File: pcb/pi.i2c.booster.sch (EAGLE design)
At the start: 41 parts, among them M328 ATMEGA328P-AU, SW1 RJ45SMD, SW2 RJ45SMD, SW3 RJ45SMD, T1 IRFR5305, T2 BC847BSMD, T3 BC847BSMD

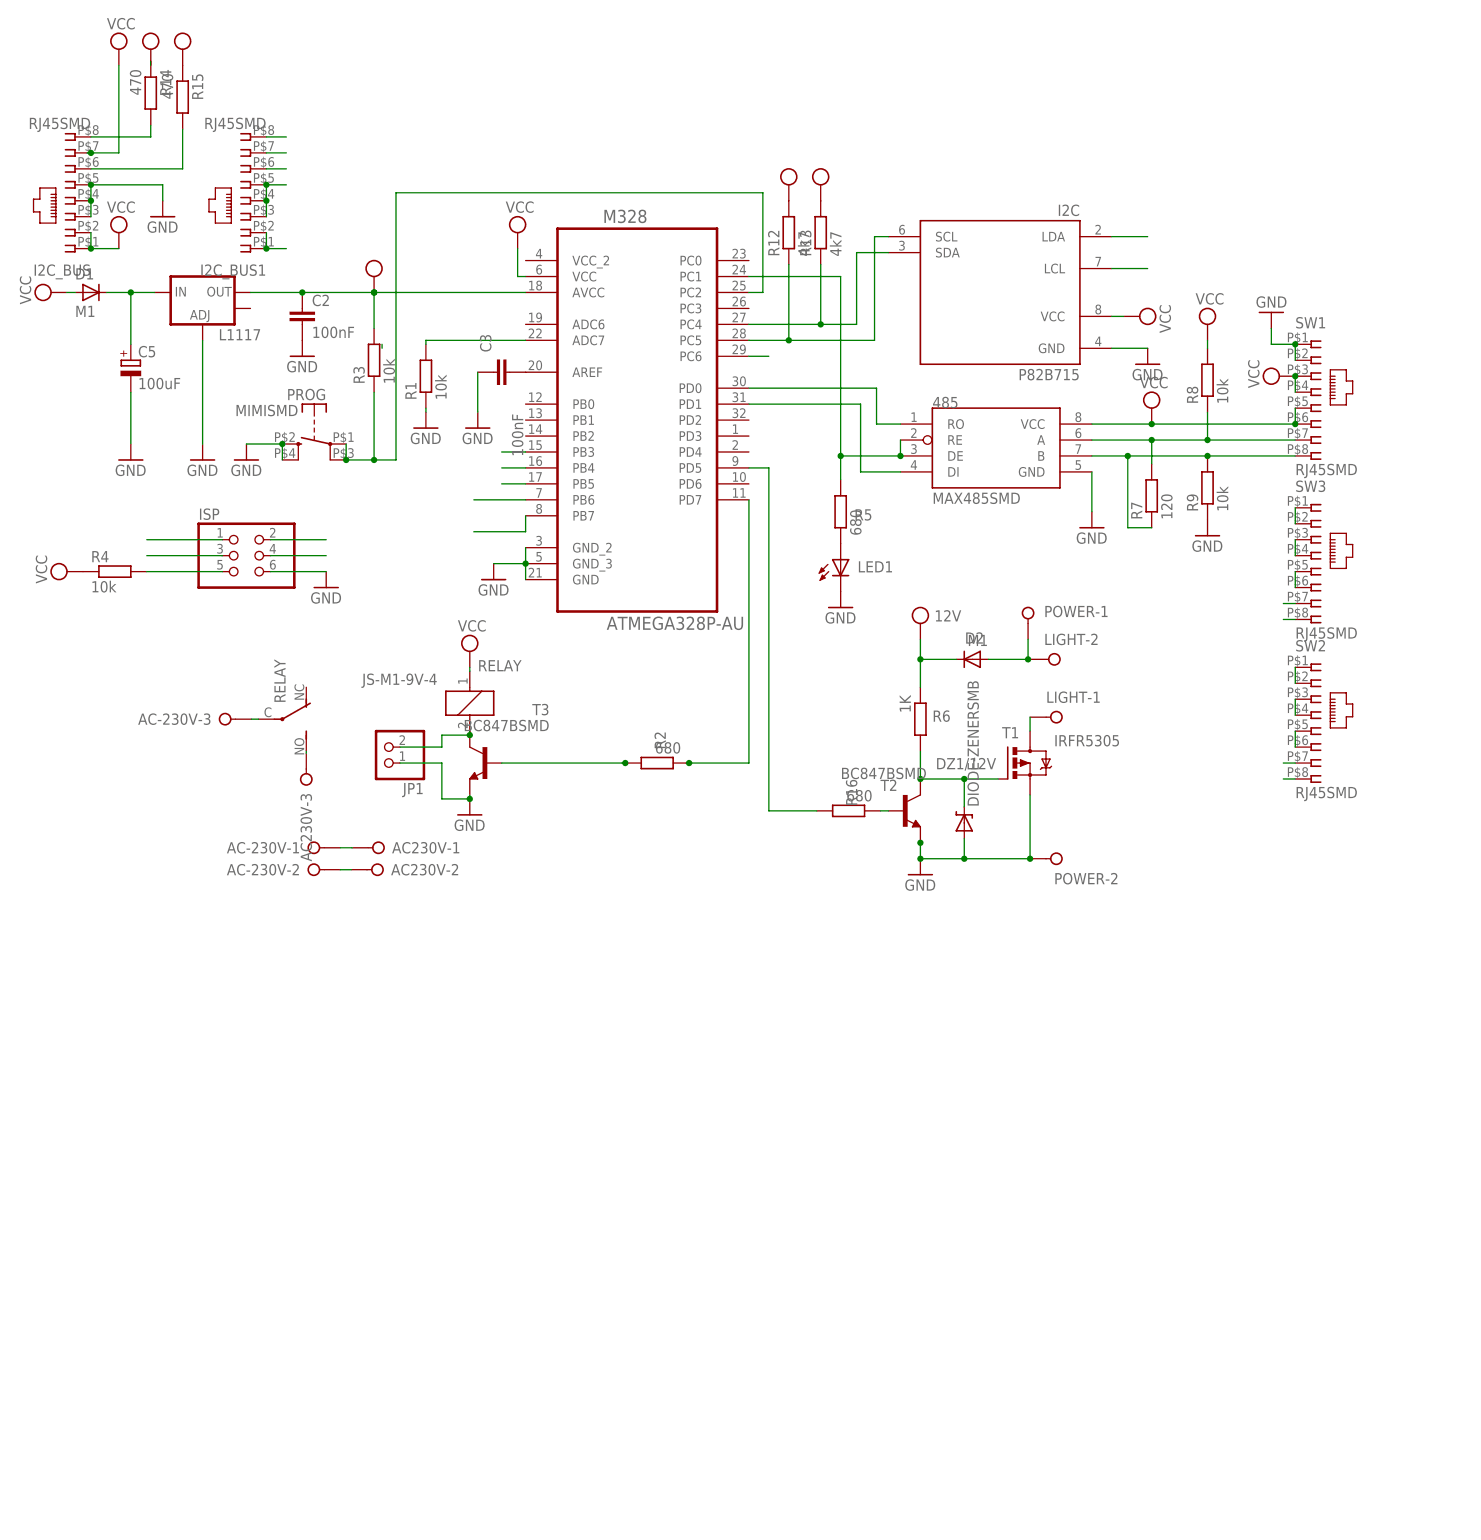
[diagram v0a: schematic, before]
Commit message: add booster
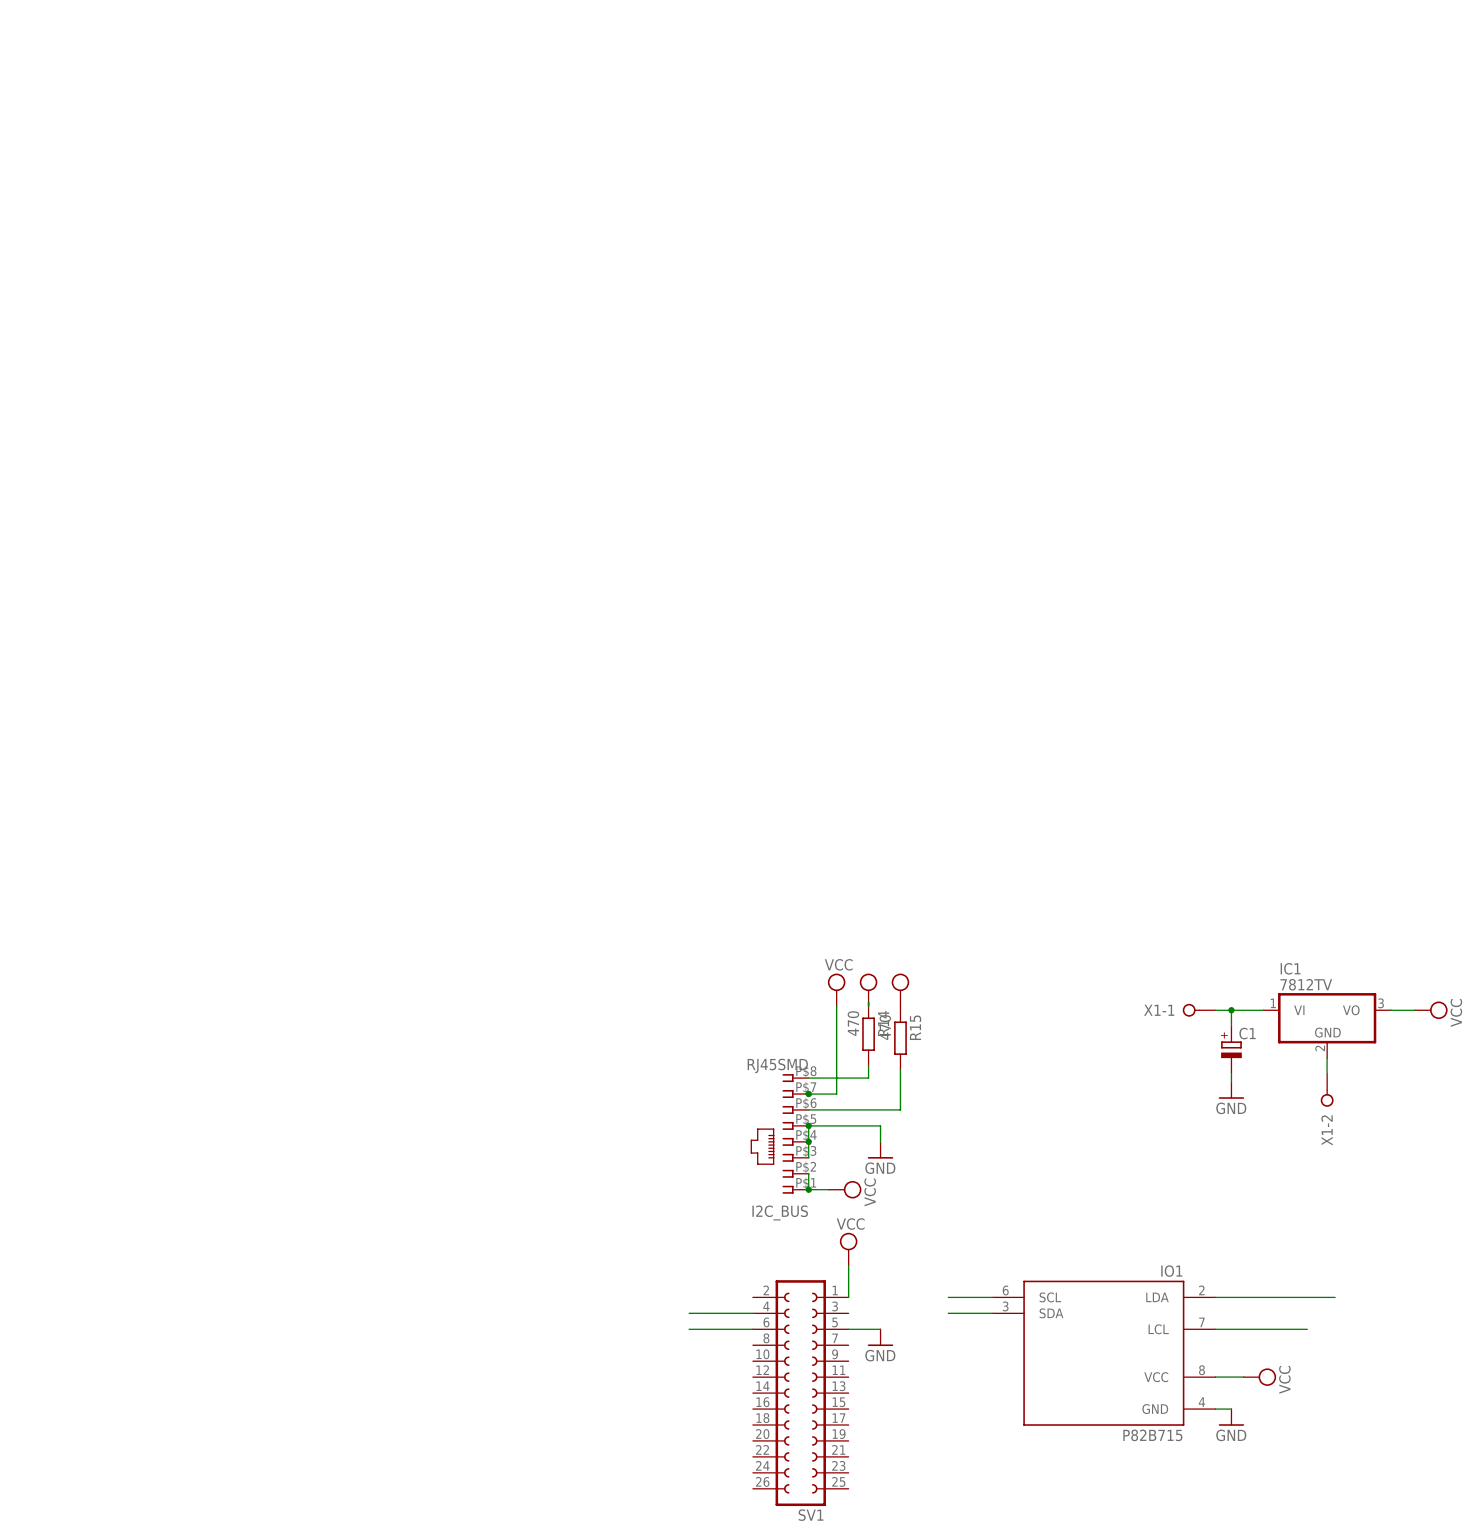
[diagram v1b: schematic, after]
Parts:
- removed 485: MAX485SMD, maxim:MAX485SMD
- removed AC-230V, AC230V: (no value), con-wago-508:W237-3E
- removed C2, C3: 100nF, rcl:C-EUC1206
- removed C5: 100uF, rcl:CPOL-EU140CLH-0810
- removed D1, D2: M1, diode:ES2D
- removed DZ1/12V: DIODE-ZENERSMB, sparkfun:DIODE-ZENERSMB
- removed I2C: P82B715, i2c:P82B715
- removed I2C_BUS1, SW1, SW2, SW3: RJ45SMD, con-tycoelectronics:RJ45SMD
- removed ISP: (no value), pinhead:PINHD-2X3
- removed JP1: (no value), pinhead:PINHD-1X2
- removed L1117: (no value), sparkfun:V_REG_LM1117SOT223
- removed LED1: (no value), led:LEDSML1206
- removed LIGHT, POWER: (no value), con-wago-508:W237-02P
- removed M328: ATMEGA328P-AU, atmega328:ATMEGA328P-AU
- removed PROG: MIMISMD, switch-misc:MIMISMD
- removed R1, R3, R4, R8, R9: 10k, rcl:R-EU_R1206
- removed R12, R13: 4k7, rcl:R-EU_R1206
- removed R16, R2, R5: 680, rcl:R-EU_R1206
- removed R6: 1K, rcl:R-EU_R1206
- removed R7: 120, rcl:R-EU_R1206
- removed RELAY: JS-M1-9V-4, relay:JS-M1-9V-4
- removed T1: IRFR5305, transistor-power:IRFR5305
- removed T2, T3: BC847BSMD, transistor-npn:BC847BSMD
- added C1: (no value), rcl:CPOL-EUB45181B
- added IC1: 7812TV, linear:7812TV
- added IO1: P82B715, i2c:P82B715
- added SV1: (no value), con-lsta:FE13-2
- added X1: (no value), con-wago-508:W237-02P
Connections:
- removed net 12V: D2.A, LIGHT-2.KL, POWER-1.KL
- removed net A: 485.A, R7.2, R8.1, SW1.7, SW2.7, SW3.7
- removed net B: 485.B, R7.1, R9.2, SW1.8, SW2.8, SW3.8
- removed net IN: C5.+, D1.C, L1117.IN
- removed net MISO: ISP.1, M328.PB4
- removed net MOSI: ISP.4, M328.PB3
- removed net N$10: AC-230V-2.KL, AC230V-2.KL
- removed net N$12: DZ1/12V.C, R6.2, T1.G, T2.C
- removed net N$13: R2.2, T3.B
- removed net N$15: LIGHT-1.KL, T1.D
- removed net N$16: AC-230V-3.KL, RELAY2.P
- removed net N$18: 485.DE, 485.RE, M328.PC1, R5.2
- removed net N$2: R16.1, T2.B
- removed net N$26: M328.ADC7, R1.2
- removed net N$33: M328.PD7, R2.1
- removed net N$36: C3.1, M328.AREF
- removed net N$4: 485.DI, M328.PD1
- removed net N$41: JP1.2, RELAY1.2, T3.C
- removed net N$48: LED1.A, R5.1
- removed net N$49: M328.PB6
- removed net N$5: 485.RO, M328.PD0
- removed net N$50: M328.PB7
- removed net N$6: M328.PC2, PROG.P, PROG.P@1, R3.1
- removed net N$7: M328.PD5, R16.2
- removed net N$8: AC230V-3.KL, RELAY2.S
- removed net N$9: AC-230V-1.KL, AC230V-1.KL
- removed net RESET: ISP.5, M328.PC6, R4.2
- removed net SCK: ISP.3, M328.PB5
- net +12V: now also C1.+, IC1.VI, X1-1.KL; no longer D1.A, D2.C, I2C_BUS1.1, I2C_BUS1.2, R6.1, SW1.3, SW1.4, SW2.3, SW2.4, SW3.3, SW3.4
- net GND: now also C1.-, IC1.GND, IO1.GND, SV1.5, X1-2.KL; no longer 485.GND, C2.2, C3.2, C5.-, DZ1/12V.A, I2C.GND, I2C_BUS1.3, I2C_BUS1.4, I2C_BUS1.5, ISP.6, JP1.1, L1117.ADJ, LED1.C, M328.GND, M328.GND_2, M328.GND_3, POWER-2.KL, PROG.S, PROG.S@1, R1.1, R9.1, SW1.1, SW1.2, SW2.1, SW2.2, SW3.1, SW3.2, T1.S, T2.E, T3.E
- net LX: now also IO1.LDA; no longer I2C.LDA, I2C_BUS1.8
- net LY: now also IO1.LCL; no longer I2C.LCL, I2C_BUS1.6
- net SCL: now also IO1.SCL, SV1.6; no longer I2C.SCL, M328.PC5, R12.1
- net SDA: now also IO1.SDA, SV1.4; no longer I2C.SDA, M328.PC4, R13.1
- net VCC: now also IC1.VO, IO1.VCC, SV1.1; no longer 485.VCC, C2.1, I2C.VCC, I2C_BUS1.7, ISP.2, L1117.OUT, M328.AVCC, M328.VCC, R12.2, R13.2, R3.2, R4.1, R8.2, RELAY1.1, SW1.5, SW1.6, SW2.5, SW2.6, SW3.5, SW3.6
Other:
- moved on the sheet: I2C_BUS, R14, R15
